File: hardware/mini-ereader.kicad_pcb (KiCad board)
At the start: 2 copper layers, 60 x 90 mm, 0 parts

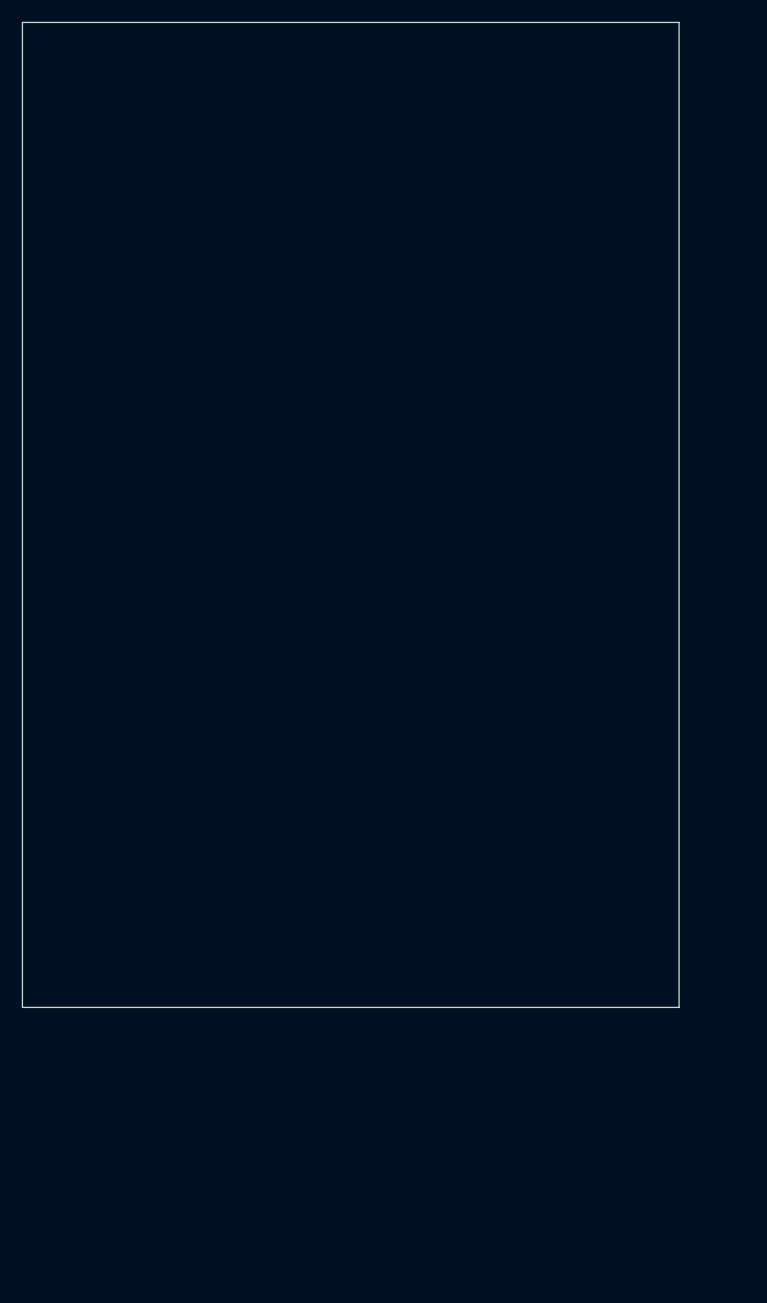
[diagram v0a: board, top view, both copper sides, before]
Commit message: Adapt repo to Mini E-Reader; add 4.26" display + frontlight + KiCad CI
Full Colophon->project adaptation and incorporation of the owner-supplied
Good Display FL0426-S01C frontlight datasheet.

Project docs (Colophon "adopt forward"):
- README.md rewritten as the Mini E-Reader Brief.
- docs/adr/0001-0005 = e-reader decisions (MCU, display+frontlight, power,
  native-USB programming, frontlight driver).
- docs/research-log.md, docs/runbook.md, CHANGELOG.md restarted for the
  project.

Display/frontlight (from FL0426-S01C):
- Corrected display to 4.26" 800x480 EPD (was a 2.13" assumption). The PDF
  is a FRONTLIGHT module, not the panel: tunable white, 2 channels of 5
  series LEDs (VF<=15V, IF<=15mA), 6-pin FPC (1 LEDC+ 2 LEDC- 3/4 NC
  5 LEDW+ 6 LEDW-).
- Added frontlight subsystem: connector J5 + 2x TPS61165 constant-current
  boost drivers, PWM-dimmed from GPIO15/16 (cold/warm). ADR 0005.
- DESIGN.md, BOM.csv, gen_netlist_skidl.py, and the KiCad scaffold updated
  (board outline ~66x115mm; sch/pcb notes).

KiCad-capable environment:
- .github/workflows/kicad.yml runs kicad-cli (kicad/kicad:8.0) ERC/DRC and
  exports a schematic PDF + gerbers as artifacts on push.

Still needed: the EPD panel's own datasheet to lock the display FPC pinout
and controller (DESIGN.md section 5, BOM J4).

Note: file deletion was blocked by the sandbox, so Colophon leftovers
remain and are pending removal: docs/adr/{0001-minimal-by-default,
0002-markdown-in-git,0003-just-in-time-over-upfront,0004-naming-conventions,
0005-coverage-mapping}.md, docs/faq.md, docs/adoption.md, and hardware/docs/
(now pointer stubs). docs/adr/ therefore has temporary duplicate numbering.

Validated: JSON parses, Python compiles, KiCad S-expressions balanced,
workflow YAML parses.

Co-Authored-By: Claude Opus 4.8 <noreply@anthropic.com>
Claude-Session: https://claude.ai/code/session_01XLMfdr5mHwD9XVwrMpqCsJ
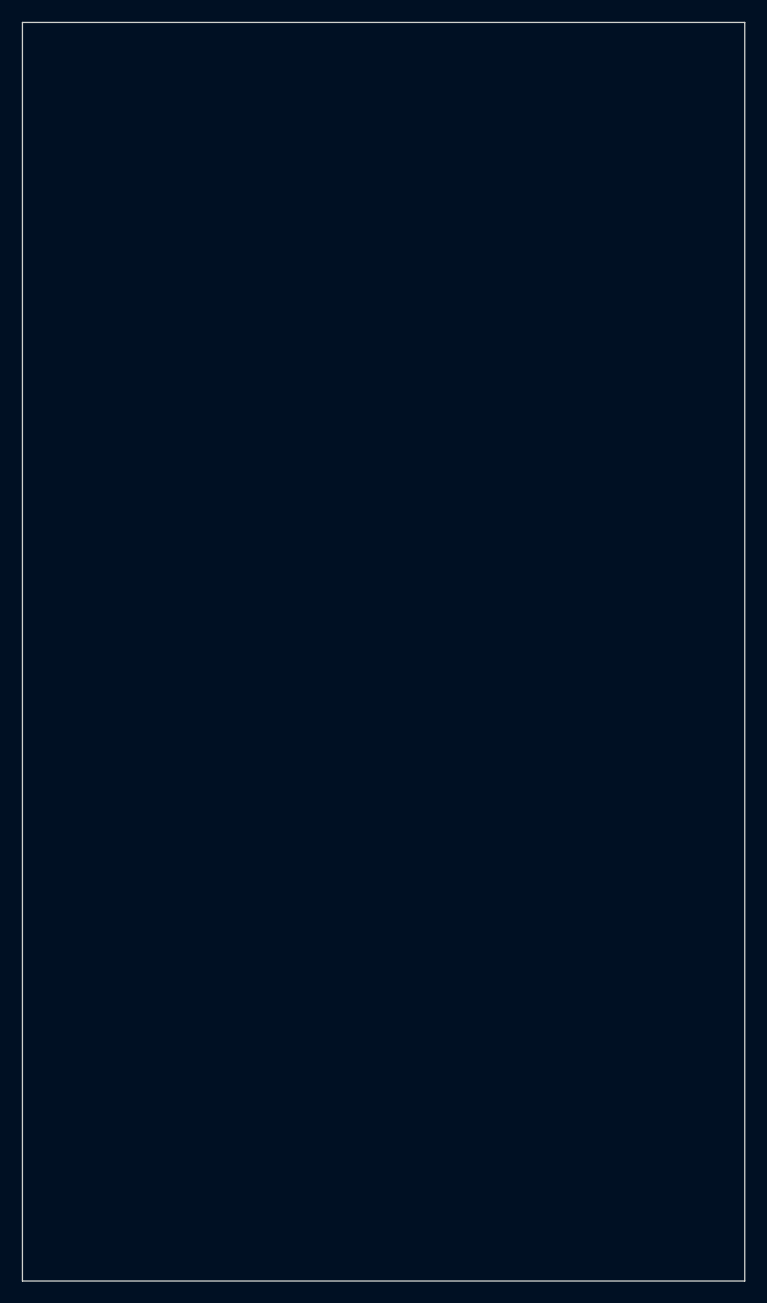
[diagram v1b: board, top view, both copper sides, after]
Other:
- board size 60 x 90 mm -> 66 x 115 mm
- board text added: "Mini E-Reader 0.1 (66x115mm placeholder) — lay out from hardware/DESIGN.md"
- board text removed: "Mini E-Reader 0.1 — lay out from hardware/DESIGN.md"
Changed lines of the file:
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@@
 		(rev "0.1")
 		(company "Craft Code Systems")
-		(comment 1 "2-layer FR-4, 1.6mm. Lay out from hardware/DESIGN.md")
+		(comment 1 "4.26in 800x480 EPD + frontlight. 2-layer FR-4 1.6mm. See hardware/DESIGN.md")
 	)
 	(layers
@@
 	(gr_line
 		(start 100 50)
-		(end 160 50)
+		(end 166 50)
 		(stroke
 			(width 0.1)
@@
 	)
 	(gr_line
-		(start 160 50)
-		(end 160 140)
+		(start 166 50)
+		(end 166 165)
 		(stroke
 			(width 0.1)
@@
 	)
 	(gr_line
-		(start 160 140)
-		(end 100 140)
+		(start 166 165)
+		(end 100 165)
 		(stroke
 			(width 0.1)
@@
 	)
 	(gr_line
-		(start 100 140)
+		(start 100 165)
 		(end 100 50)
 		(stroke
@@
 		(layer "Edge.Cuts")
 	)
-	(gr_text "Mini E-Reader 0.1 — lay out from hardware/DESIGN.md"
+	(gr_text "Mini E-Reader 0.1 (66x115mm placeholder) — lay out from hardware/DESIGN.md"
 		(at 101 48)
 		(layer "Cmts.User")
